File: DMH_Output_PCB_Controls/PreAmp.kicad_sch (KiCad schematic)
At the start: 37 parts, among them U16 NE5532, U17 NE5532, U18 NE5532, U19 NE5532

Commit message: Starting Controls PCB design
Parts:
- added J13: Conn_01x06, Connector_PinSocket_2.54mm:PinSocket_1x06_P2.54mm_Vertical, symbol Connector_Generic:Conn_01x06
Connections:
- net RV3B_p4: now reaches C35.2, R73.2, R79.1, RV3.4, U19.1
- net RV3B_p4: now also J13.4 (Pin_4)
- net RV3A_p1: now reaches C19.2, R68.2, R76.1, RV3.1, U17.1
- net RV3A_p1: now also J13.1 (Pin_1)
- net RV3A_p2: now reaches C21.1, RV3.2
- net RV3A_p2: now also J13.2 (Pin_2)
- net RV3A_p3: now reaches C37.2, RV3.3
- net RV3A_p3: now also J13.3 (Pin_3)
- net RV3B_p5: now reaches C20.1, RV3.5
- net RV3B_p5: now also J13.5 (Pin_5)
- net RV3B_p6: now reaches C38.2, RV3.6
- net RV3B_p6: now also J13.6 (Pin_6)

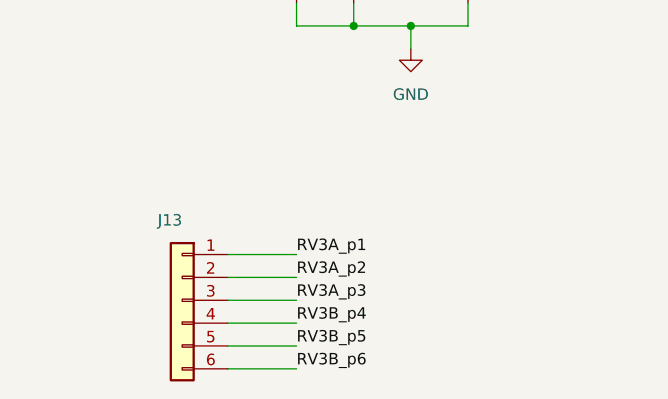
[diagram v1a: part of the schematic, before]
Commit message: Controls PCB placement ongoing
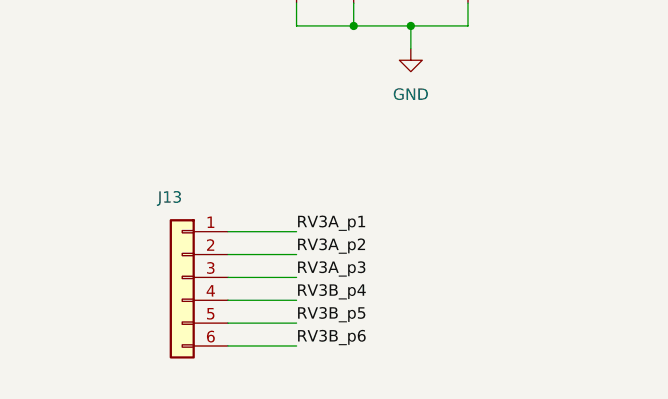
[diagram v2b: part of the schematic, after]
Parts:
- RV3: Function (none) -> Ext Volume
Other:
- moved on the sheet: J13

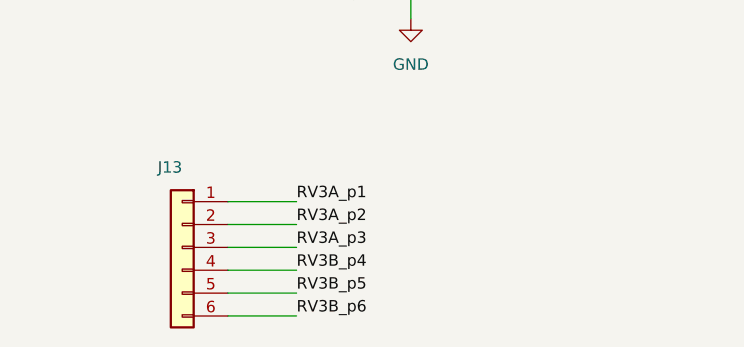
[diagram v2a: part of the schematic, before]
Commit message: Controls PCB comp placement done
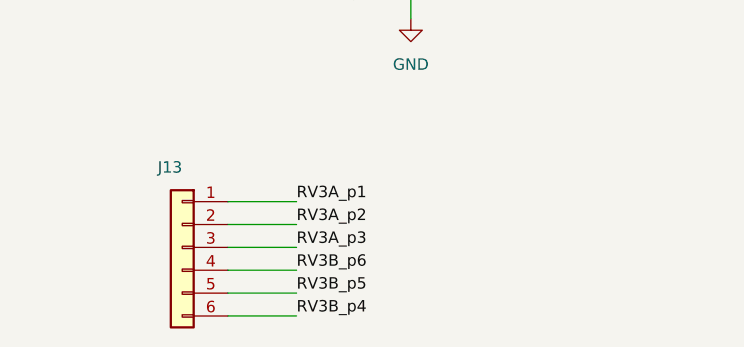
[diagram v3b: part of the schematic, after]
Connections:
- net RV3B_p4: now also J13.6 (Pin_6); no longer J13.4 (Pin_4)
- net RV3B_p6: now also J13.4 (Pin_4); no longer J13.6 (Pin_6)
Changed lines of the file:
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@@
 	)
 	(label "RV3B_p4"
-		(at 50.8 144.78 0)
+		(at 50.8 149.86 0)
 		(effects
 			(font
@@
 	)
 	(label "RV3B_p6"
-		(at 50.8 149.86 0)
+		(at 50.8 144.78 0)
 		(effects
 			(font

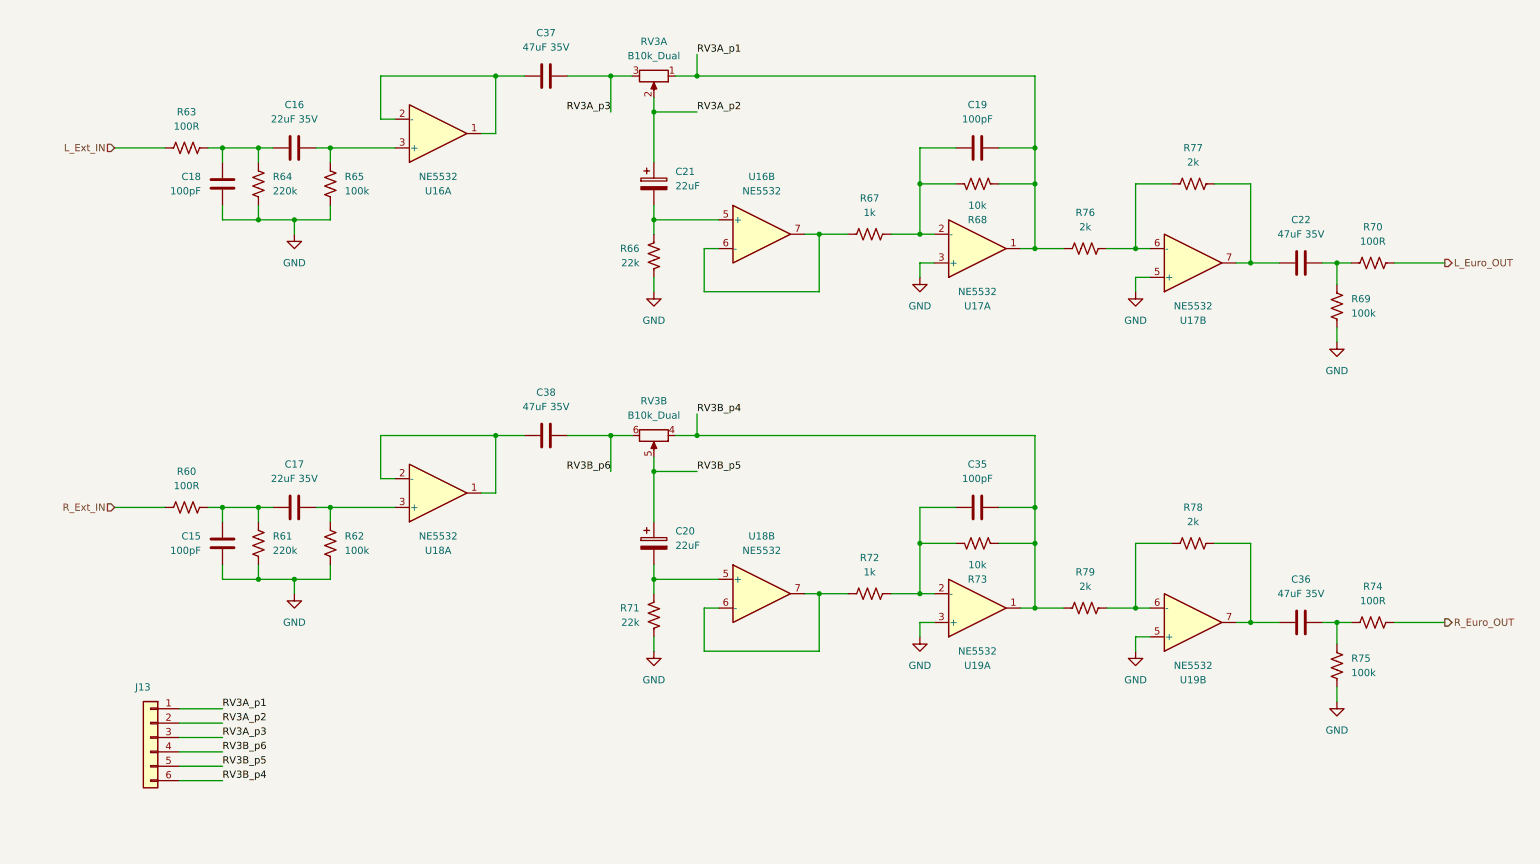
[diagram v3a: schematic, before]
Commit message: Clarified interPCB connectors in schematic
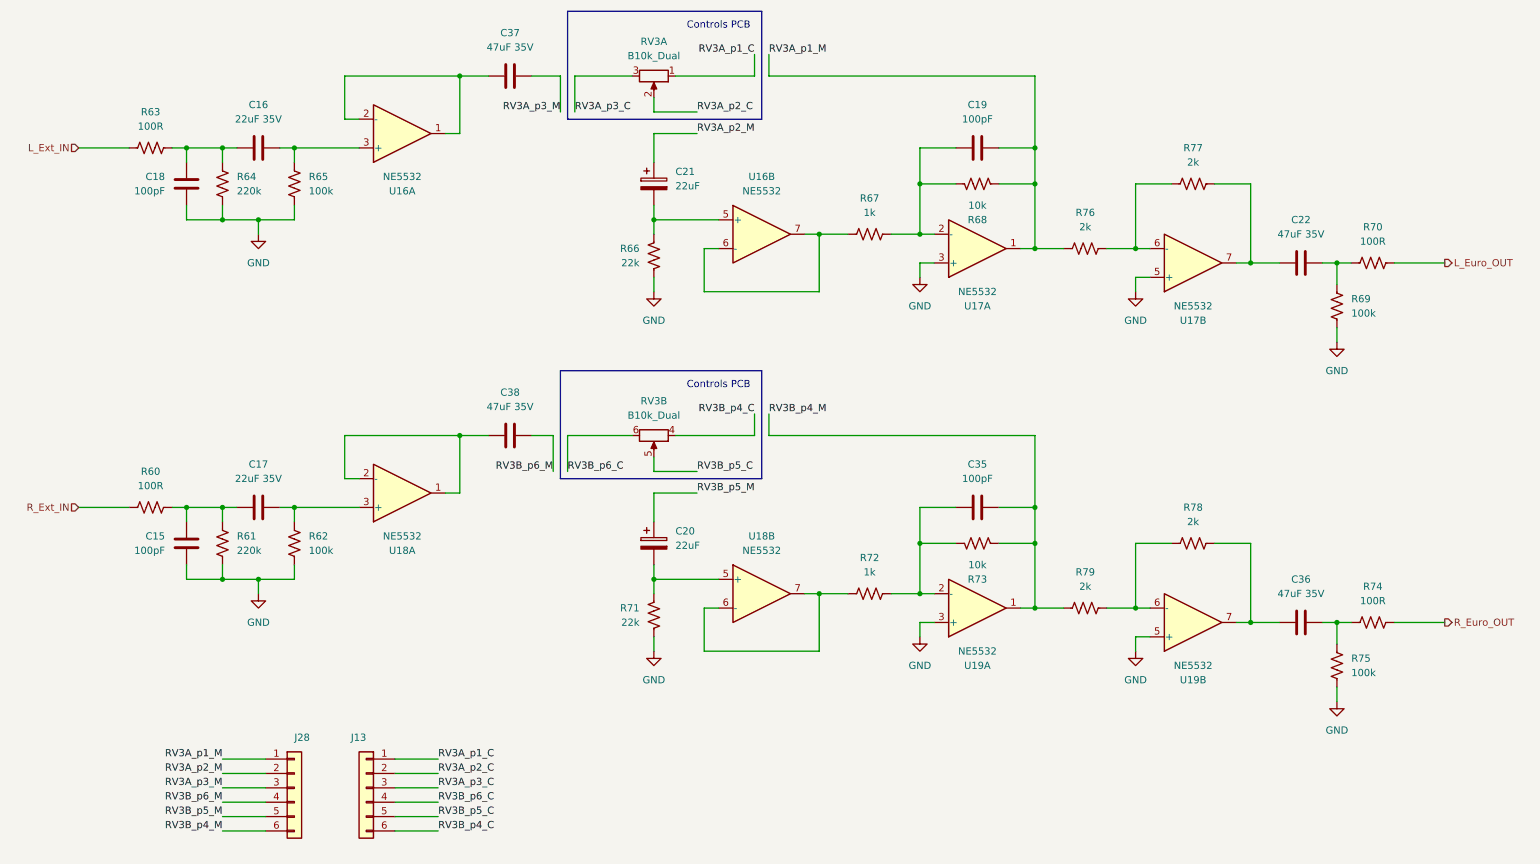
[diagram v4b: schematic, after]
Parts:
- added J28: Conn_01x06, Connector_PinHeader_2.54mm:PinHeader_1x06_P2.54mm_Vertical, symbol Connector_Generic:Conn_01x06
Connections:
- net RV3A_p1 renamed RV3A_p1_M
- net RV3A_p1_M: now also J28.1 (Pin_1); no longer J13.1 (Pin_1), RV3.1
- net RV3A_p2 renamed RV3A_p2_C
- net RV3A_p2_C: no longer C21.1
- net RV3A_p3 renamed RV3A_p3_C
- net RV3A_p3_C: no longer C37.2
- net RV3B_p4 renamed RV3B_p4_M
- net RV3B_p4_M: now also J28.6 (Pin_6); no longer J13.6 (Pin_6), RV3.4
- net RV3B_p5 renamed RV3B_p5_C
- net RV3B_p5_C: no longer C20.1
- net RV3B_p6 renamed RV3B_p6_C
- net RV3B_p6_C: no longer C38.2
- new net RV3A_p1_C: J13.1 (Pin_1), RV3.1
- new net RV3A_p2_M: C21.1, J28.2 (Pin_2)
- new net RV3A_p3_M: C37.2, J28.3 (Pin_3)
- new net RV3B_p4_C: J13.6 (Pin_6), RV3.4
- new net RV3B_p5_M: C20.1, J28.5 (Pin_5)
- new net RV3B_p6_M: C38.2, J28.4 (Pin_4)
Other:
- note added: "Controls PCB"
- moved on the sheet: C15, C16, C17, C18, C37, C38, J13, R60, R61, R62, R63, R64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

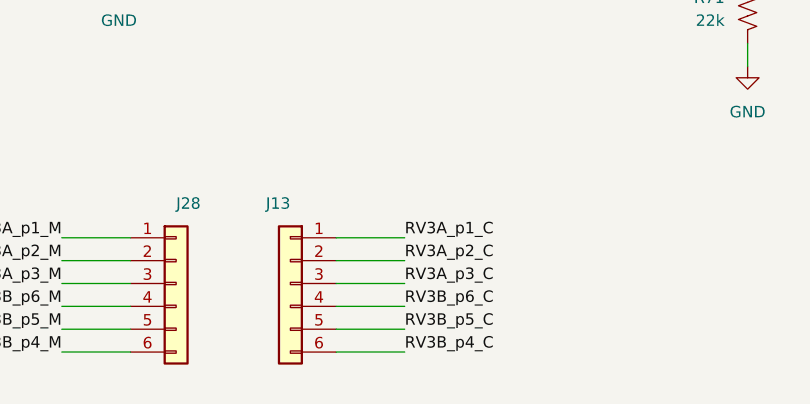
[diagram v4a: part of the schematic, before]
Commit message: Controls PCB routing in progress
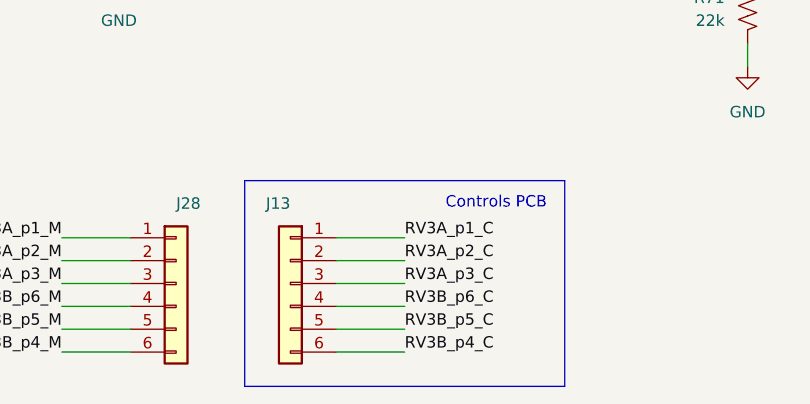
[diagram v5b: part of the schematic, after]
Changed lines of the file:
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@@
+	)
+	(rectangle
+		(start 71.12 139.7)
+		(end 106.68 162.56)
+		(stroke
+			(width 0)
+			(type default)
+		)
+		(fill
+			(type none)
+		)
 	)
 	(rectangle
@@
 		(effects
 			(font
+				(size 1.27 1.27)
+			)
+		)
+	)
+	(text "Controls PCB"
+		(exclude_from_sim no)
+		(at 99.06 142.24 0)
+		(effects
+			(font

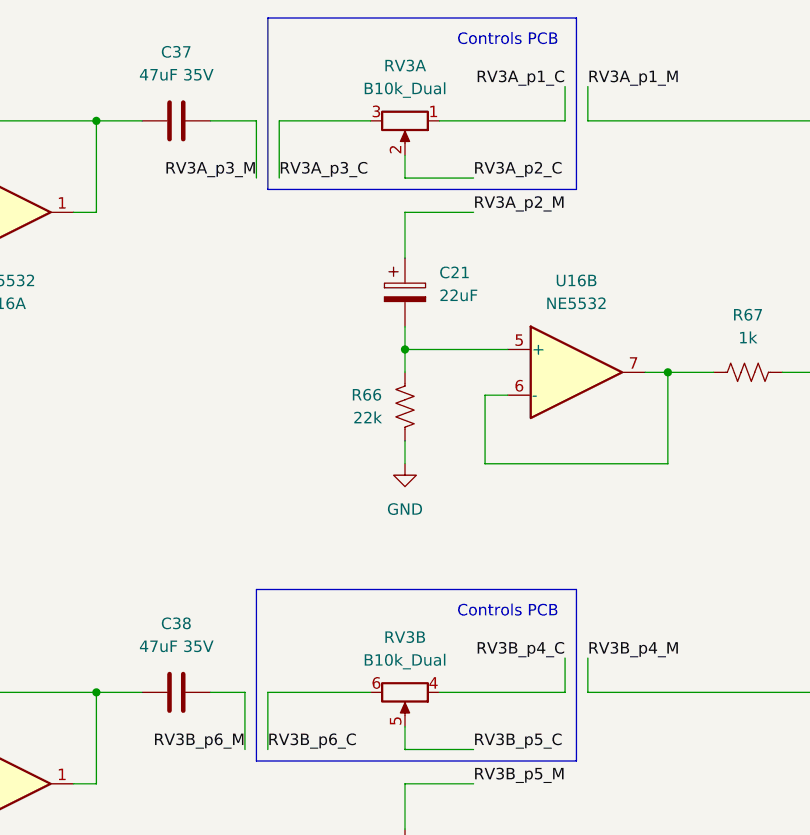
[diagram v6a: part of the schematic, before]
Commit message: Replaced jack symbols with 5pin ones
Also updated Meter LED current source resistor to 75R
Also increased LED guiding PCB mounting holes to M2.5
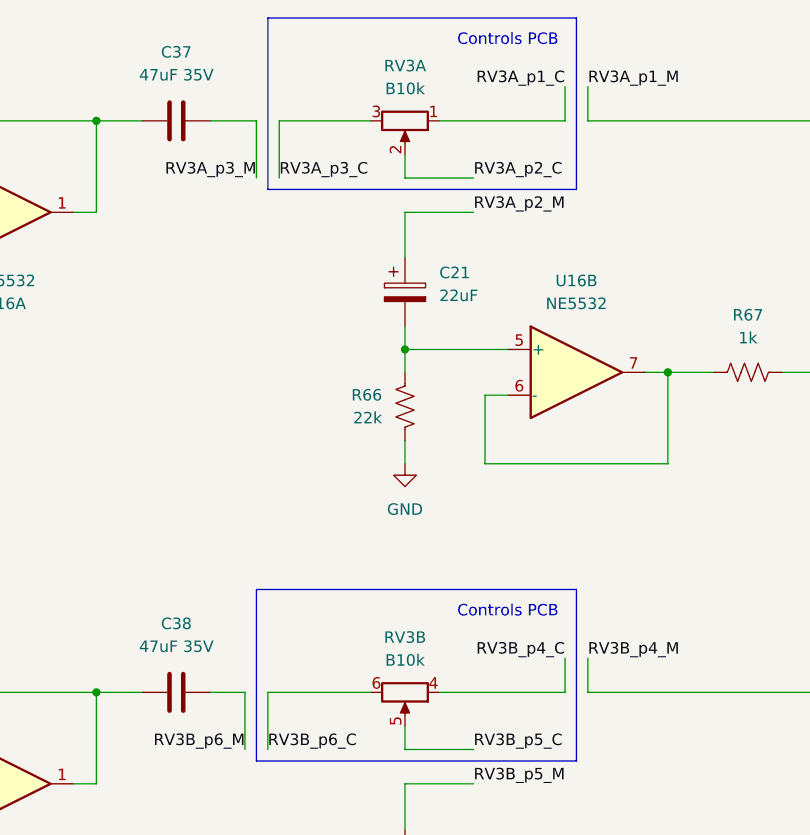
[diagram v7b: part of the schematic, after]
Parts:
- RV3: value B10k_Dual -> B10k; footprint Potentiometer_THT:Potentiometer_Alpha_RD902F-40-00D_Dual_Vertical -> SynthStuff:Potentiometer_Alpha_RD902F-40-00D_Dual_Vertical
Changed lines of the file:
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@@
 			)
 		)
-		(property "Value" "B10k_Dual"
+		(property "Value" "B10k"
 			(at 127 21.844 90)
 			(show_name no)
@@
 			)
 		)
-		(property "Footprint" "Potentiometer_THT:Potentiometer_Alpha_RD902F-40-00D_Dual_Vertical"
+		(property "Footprint" "SynthStuff:Potentiometer_Alpha_RD902F-40-00D_Dual_Vertical"
 			(at 127 25.4 0)
 			(hide yes)
@@
 					(bold yes)
 					(italic yes)
+				)
+			)
+		)
+		(property "Sim.Library" "${KICAD9_SYMBOL_DIR}/Simulation_SPICE.sp"
+			(at 127 25.4 0)
+			(hide yes)
+			(show_name no)
+			(do_not_autoplace no)
+			(effects
+				(font
+					(size 1.27 1.27)
+				)
+			)
+		)
+		(property "Sim.Name" "pot_dual"
+			(at 127 25.4 0)
+			(hide yes)
+			(show_name no)
+			(do_not_autoplace no)
+			(effects
+				(font
+					(size 1.27 1.27)
+				)
+			)
+		)
+		(property "Sim.Device" "SUBCKT"
+			(at 127 25.4 0)
+			(hide yes)
+			(show_name no)
+			(do_not_autoplace no)
+			(effects
+				(font
+					(size 1.27 1.27)
+				)
+			)
+		)
+		(property "Sim.Pins" "1=r1A 2=wA 3=r0A 4=r1B 5=wB 6=r0B"
+			(at 127 25.4 0)
+			(hide yes)
+			(show_name no)
+			(do_not_autoplace no)
+			(effects
+				(font
+					(size 1.27 1.27)
+				)
+			)
+		)
+		(property "Sim.Params" "Rtot=1 wpos=0.4"
+			(at 127 25.4 0)
+			(hide yes)
+			(show_name no)
+			(do_not_autoplace no)
+			(effects
+				(font
+					(size 1.27 1.27)
 				)
 			)
@@
 			)
 		)
-		(property "Value" "B10k_Dual"
+		(property "Value" "B10k"
 			(at 127 85.344 90)
 			(show_name no)
@@
 			)
 		)
-		(property "Footprint" "Potentiometer_THT:Potentiometer_Alpha_RD902F-40-00D_Dual_Vertical"
+		(property "Footprint" "SynthStuff:Potentiometer_Alpha_RD902F-40-00D_Dual_Vertical"
 			(at 127 88.9 0)
 			(hide yes)
@@
 				)
 			)
+		)
+		(property "Sim.Library" "${KICAD9_SYMBOL_DIR}/Simulation_SPICE.sp"
+			(at 127 88.9 0)
+			(hide yes)
+			(show_name no)
+			(do_not_autoplace no)
+			(effects
+				(font
+					(size 1.27 1.27)
+				)
+			)
+		)
+		(property "Sim.Name" "pot_dual"
+			(at 127 88.9 0)
+			(hide yes)
+			(show_name no)
+			(do_not_autoplace no)
+			(effects
+				(font
+					(size 1.27 1.27)
+				)
+			)
+		)
+		(property "Sim.Device" "SUBCKT"
+			(at 127 88.9 0)
+			(hide yes)
+			(show_name no)
+			(do_not_autoplace no)
+			(effects
+				(font
+					(size 1.27 1.27)
+				)
+			)
+		)
+		(property "Sim.Pins" "1=r1A 2=wA 3=r0A 4=r1B 5=wB 6=r0B"
+			(at 127 88.9 0)
+			(hide yes)
+			(show_name no)
+			(do_not_autoplace no)
+			(effects
+				(font
+					(size 1.27 1.27)
+				)
+			)
+		)
+		(property "Sim.Params" "Rtot=1 wpos=0.4"
+			(at 127 88.9 0)
+			(hide yes)
+			(show_name no)
+			(do_not_autoplace no)
+			(effects
+				(font
+					(size 1.27 1.27)
+				)
+			)
